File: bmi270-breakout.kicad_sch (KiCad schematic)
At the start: 14 parts, among them CN1 AFC10-S04QCA-00, CN2 AFC10-S04QCA-00, J1 Conn_01x07_Pin, J2 Conn_01x05_Pin, U1 BMI270

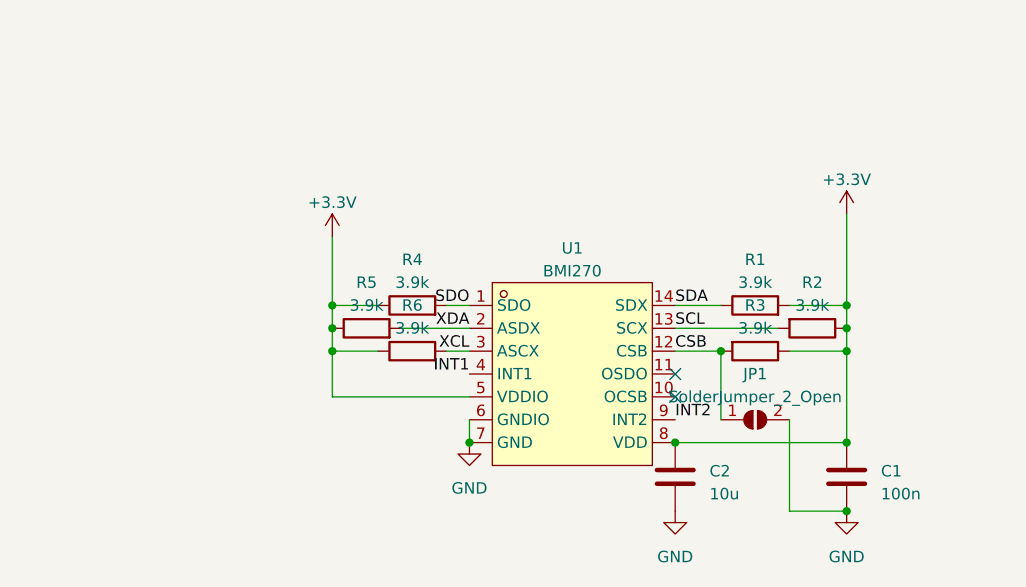
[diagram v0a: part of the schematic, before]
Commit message: documentation, migrate to kicad 8, fix address jumper, add branding
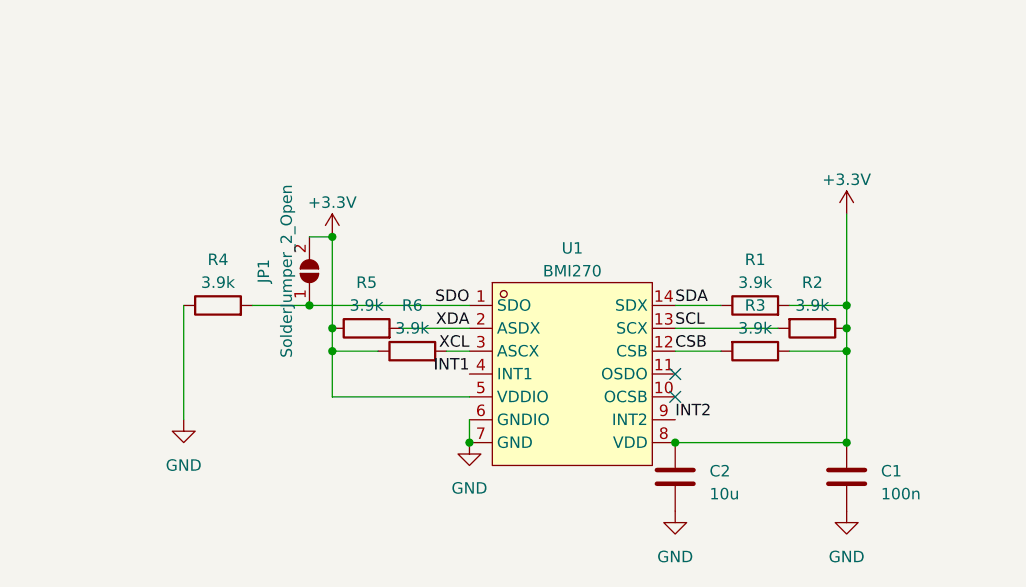
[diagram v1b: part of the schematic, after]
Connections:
- net +3.3V: now also JP1.2 (B); no longer R4.1
- net CSB: no longer JP1.1 (A)
- net GND: now also R4.1; no longer JP1.2 (B)
- net SDO: now also JP1.1 (A)
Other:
- moved on the sheet: R4

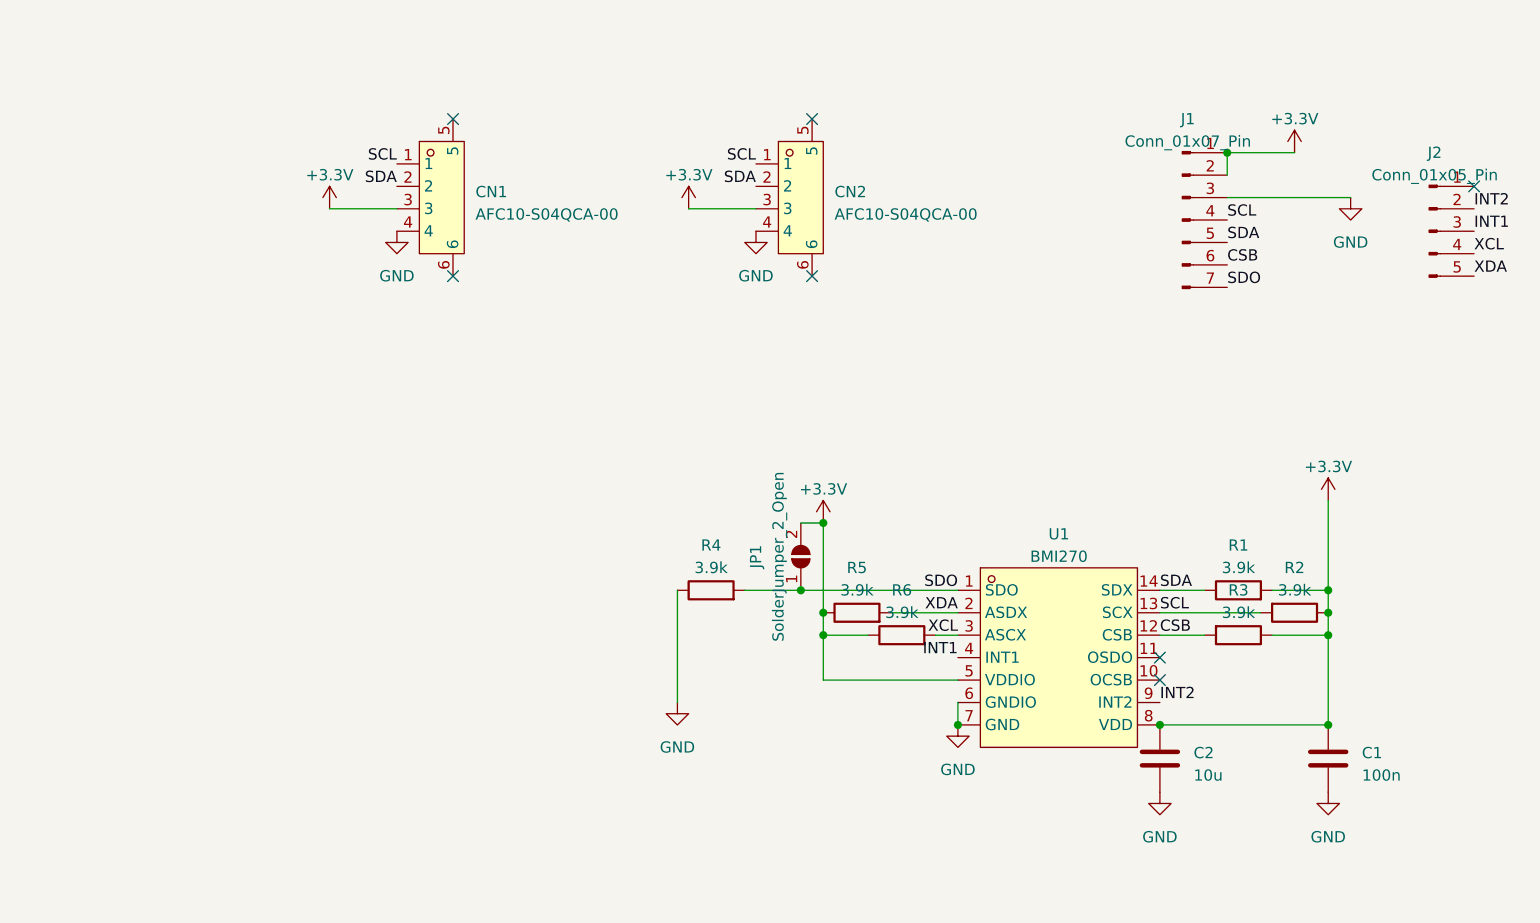
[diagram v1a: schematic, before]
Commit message: fix qwiic pinout, rework footprint
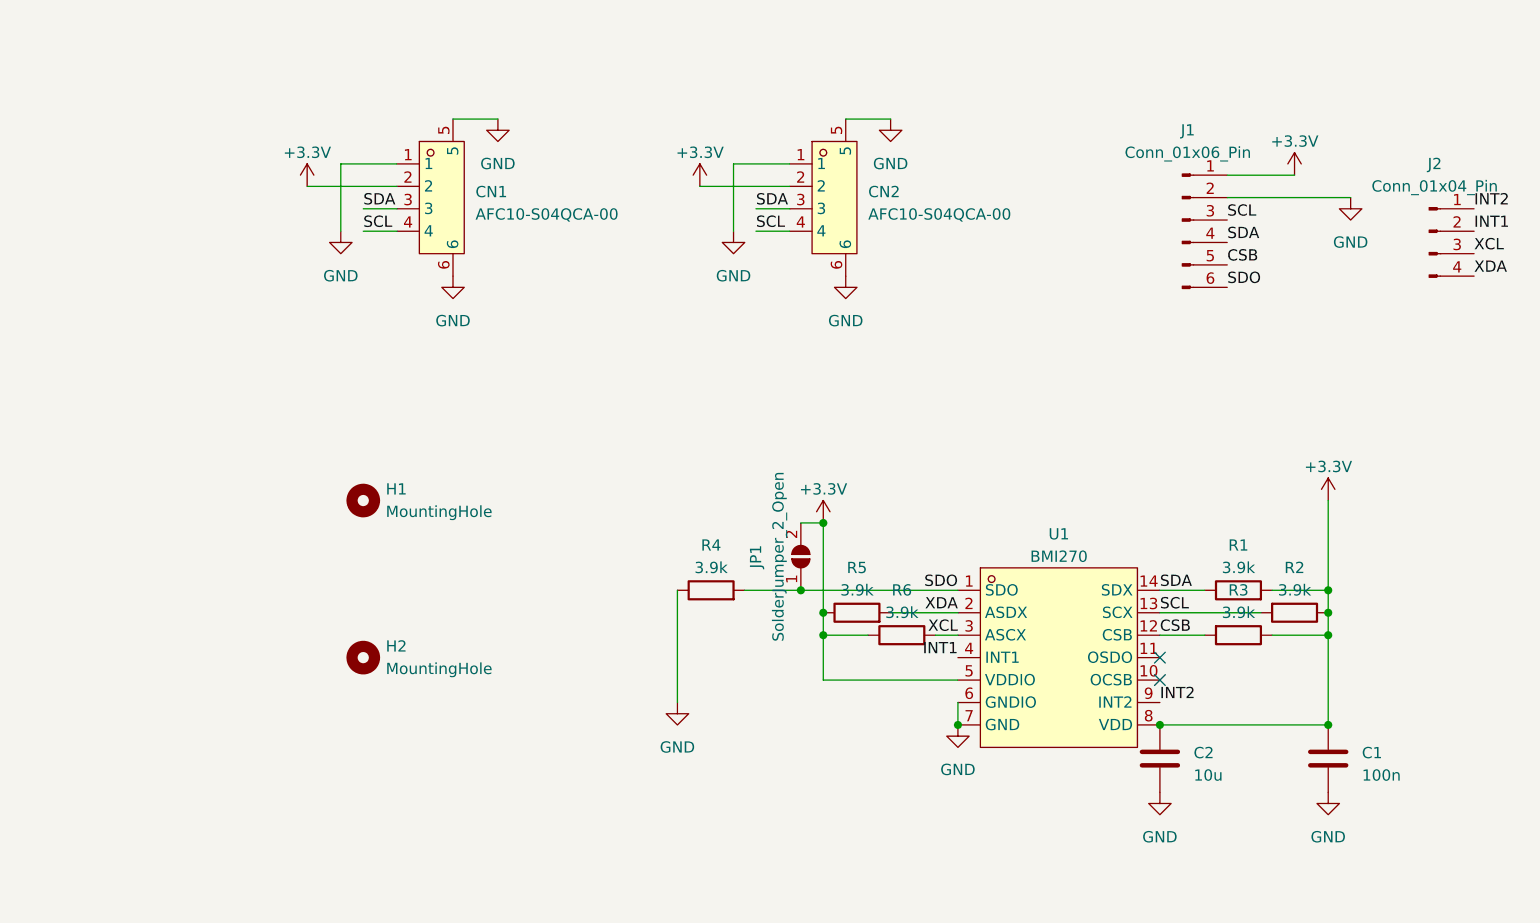
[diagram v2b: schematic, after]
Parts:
- removed J1: Conn_01x07_Pin, Connector_PinHeader_2.54mm:PinHeader_1x07_P2.54mm_Vertical, symbol Connector:Conn_01x07_Pin
- removed J2: Conn_01x05_Pin, Connector_PinHeader_2.54mm:PinHeader_1x05_P2.54mm_Vertical, symbol Connector:Conn_01x05_Pin
- added H1, H2: MountingHole, MountingHole:MountingHole_2.2mm_M2, symbol Mechanical:MountingHole
- added J1: Conn_01x06_Pin, Connector_PinHeader_2.54mm:PinHeader_1x06_P2.54mm_Vertical, symbol Connector:Conn_01x06_Pin
- added J2: Conn_01x04_Pin, Connector_PinHeader_2.54mm:PinHeader_1x04_P2.54mm_Vertical, symbol Connector:Conn_01x04_Pin
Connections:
- net +3.3V: now also CN1.2, CN2.2, J1.1 (Pin_1); no longer CN1.3, CN2.3
- net CSB: now also J1.5 (Pin_5)
- net GND: now also CN1.1, CN1.5, CN1.6, CN2.1, CN2.5, CN2.6, J1.2 (Pin_2); no longer CN1.4, CN2.4
- net INT1: now also J2.2 (Pin_2)
- net INT2: now also J2.1 (Pin_1)
- net SCL: now also CN1.4, CN2.4, J1.3 (Pin_3); no longer CN1.1, CN2.1
- net SDA: now also CN1.3, CN2.3, J1.4 (Pin_4); no longer CN1.2, CN2.2
- net SDO: now also J1.6 (Pin_6)
- net XCL: now also J2.3 (Pin_3)
- net XDA: now also J2.4 (Pin_4)
- no-connect marks 7 -> 2

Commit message: use higher pullup, refine schematic
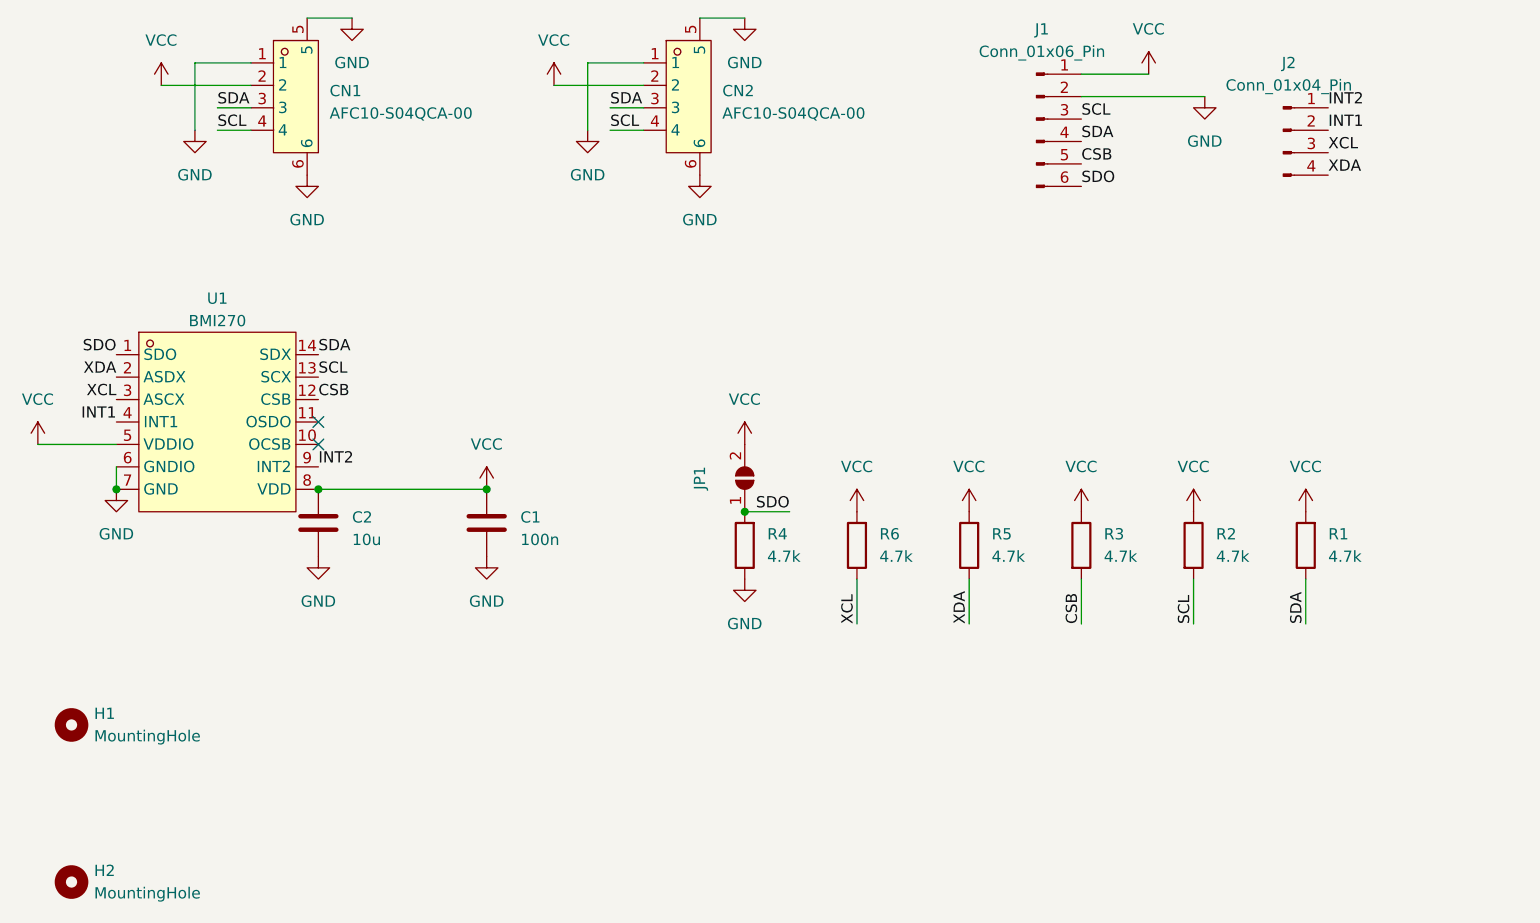
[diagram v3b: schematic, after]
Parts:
- JP1: now left out of the parts list
- R1, R2, R3, R4, R5, R6: value 3.9k -> 4.7k
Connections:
- net XCL: now also R6.1; no longer R6.2
- net XDA: now also R5.1; no longer R5.2
- net +3.3V renamed VCC
- net VCC: now also R5.2, R6.2; no longer R5.1, R6.1
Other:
- moved on the sheet: C1, C2, CN1, CN2, H1, H2, J1, J2, JP1, R1, R2, R3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

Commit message: silkscreen
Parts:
- R3, R4: value 4.7k -> 10k
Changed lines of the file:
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@@
 			)
 		)
-		(property "Value" "4.7k"
+		(property "Value" "10k"
 			(at 142.24 90.1699 0)
 			(effects
@@
 			)
 		)
-		(property "Value" "4.7k"
+		(property "Value" "10k"
 			(at 104.14 90.1699 0)
 			(effects
